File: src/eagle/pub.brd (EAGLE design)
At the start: 63.5 x 63.5 mm, 27 parts, among them IC1 PIC18F25K50, SW1 EC12E_SW

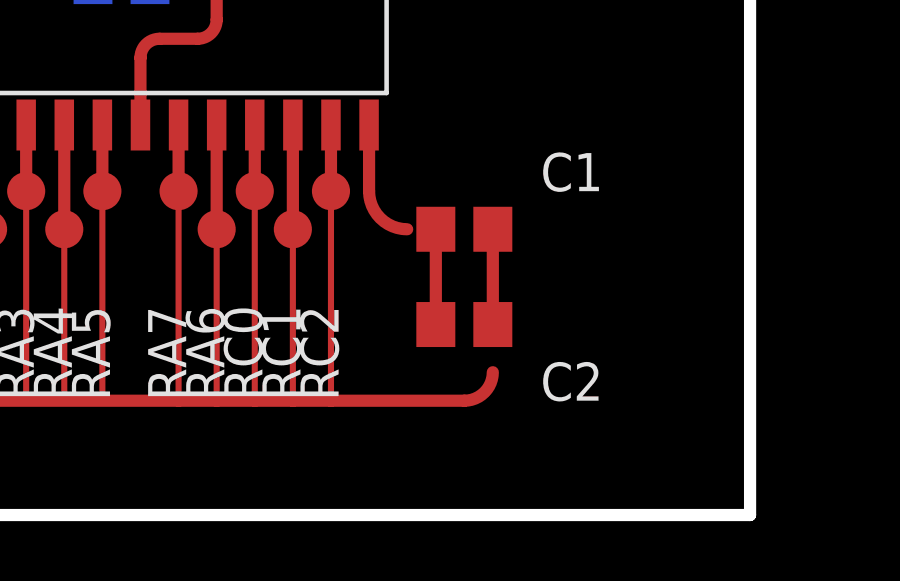
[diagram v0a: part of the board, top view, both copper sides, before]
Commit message: Fixed unconnected trace on PCB. The ITEAD guys found it. I don't know how it missed that.
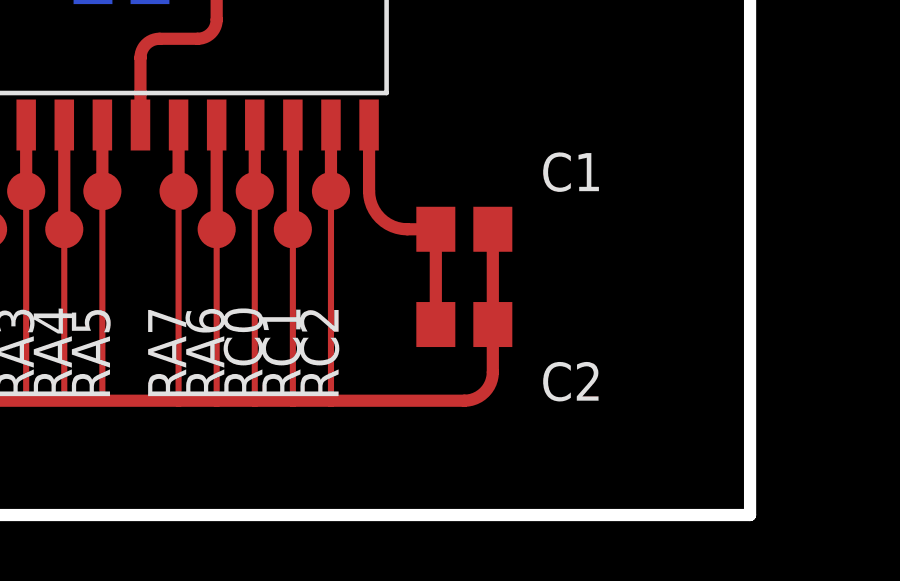
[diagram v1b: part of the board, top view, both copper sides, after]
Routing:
- net GND: track 252.9 -> 254.5 mm
- net N$3: track 7.18 -> 8.13 mm
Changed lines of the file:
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@@
 <layer number="17" name="Pads" color="2" fill="1" visible="yes" active="yes"/>
 <layer number="18" name="Vias" color="12" fill="1" visible="yes" active="yes"/>
-<layer number="19" name="Unrouted" color="6" fill="1" visible="no" active="yes"/>
+<layer number="19" name="Unrouted" color="6" fill="1" visible="yes" active="yes"/>
 <layer number="20" name="Dimension" color="15" fill="1" visible="yes" active="yes"/>
 <layer number="21" name="tPlace" color="15" fill="1" visible="no" active="yes"/>
@@
 <via x="38.1" y="31.75" extent="1-16" drill="0.4064"/>
 <wire x1="38.1" y1="31.75" x2="32.9" y2="31.75" width="0.4064" layer="16"/>
-<wire x1="54.925" y1="4.76" x2="53.975" y2="3.81" width="0.4064" layer="1" curve="-90"/>
 <wire x1="45.72" y1="16.51" x2="45.72" y2="17.78" width="0.4064" layer="1"/>
 <contactref element="JP1" pad="5"/>
@@
 <contactref element="IC1" pad="8"/>
 <wire x1="43.18" y1="13" x2="43.18" y2="15.24" width="0.4064" layer="1"/>
-<wire x1="43.18" y1="13" x2="44.45" y2="13" width="0" layer="19" extent="1-1"/>
+<wire x1="53.975" y1="3.81" x2="54.925" y2="4.76" width="0.4064" layer="1" curve="90"/>
+<wire x1="54.925" y1="4.76" x2="54.925" y2="6.35" width="0.4064" layer="1"/>
+<wire x1="44.45" y1="13" x2="43.18" y2="13" width="0" layer="19" extent="1-1"/>
 </signal>
 <signal name="N$1">
@@
 <wire x1="50.8" y1="10.795" x2="52.07" y2="9.525" width="0.4064" layer="1" curve="90"/>
 <wire x1="53.025" y1="9.525" x2="53.025" y2="6.35" width="0.4064" layer="1"/>
-<wire x1="53.025" y1="9.525" x2="52.07" y2="9.525" width="0" layer="19" extent="1-1"/>
+<wire x1="52.07" y1="9.525" x2="53.025" y2="9.525" width="0.4064" layer="1"/>
 </signal>
 </signals>

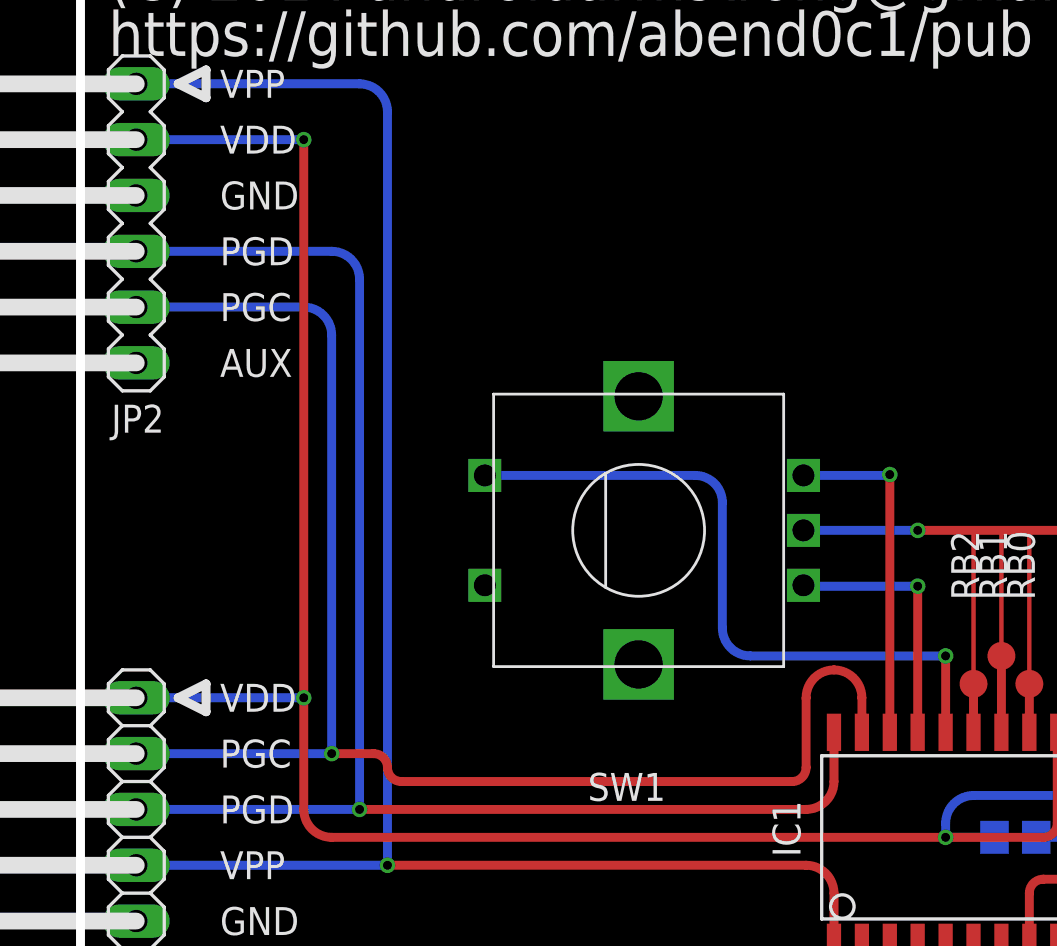
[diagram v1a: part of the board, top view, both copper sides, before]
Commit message: Reworked PCB layout and changed to vector fonts
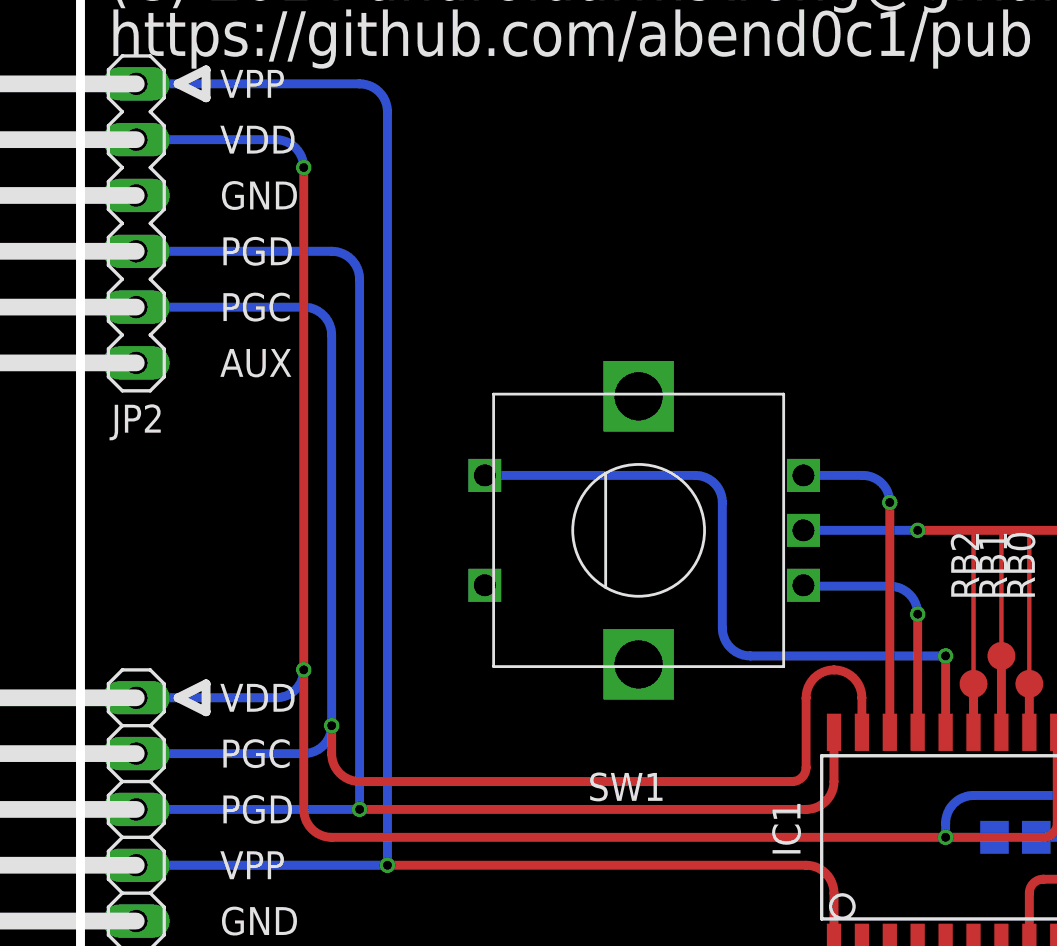
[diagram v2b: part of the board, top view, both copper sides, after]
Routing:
- net N$2: track 11.9 -> 11.1 mm
- net N$1: track 15.7 -> 14.9 mm
- net N$8: track 68.1 -> 68.6 mm

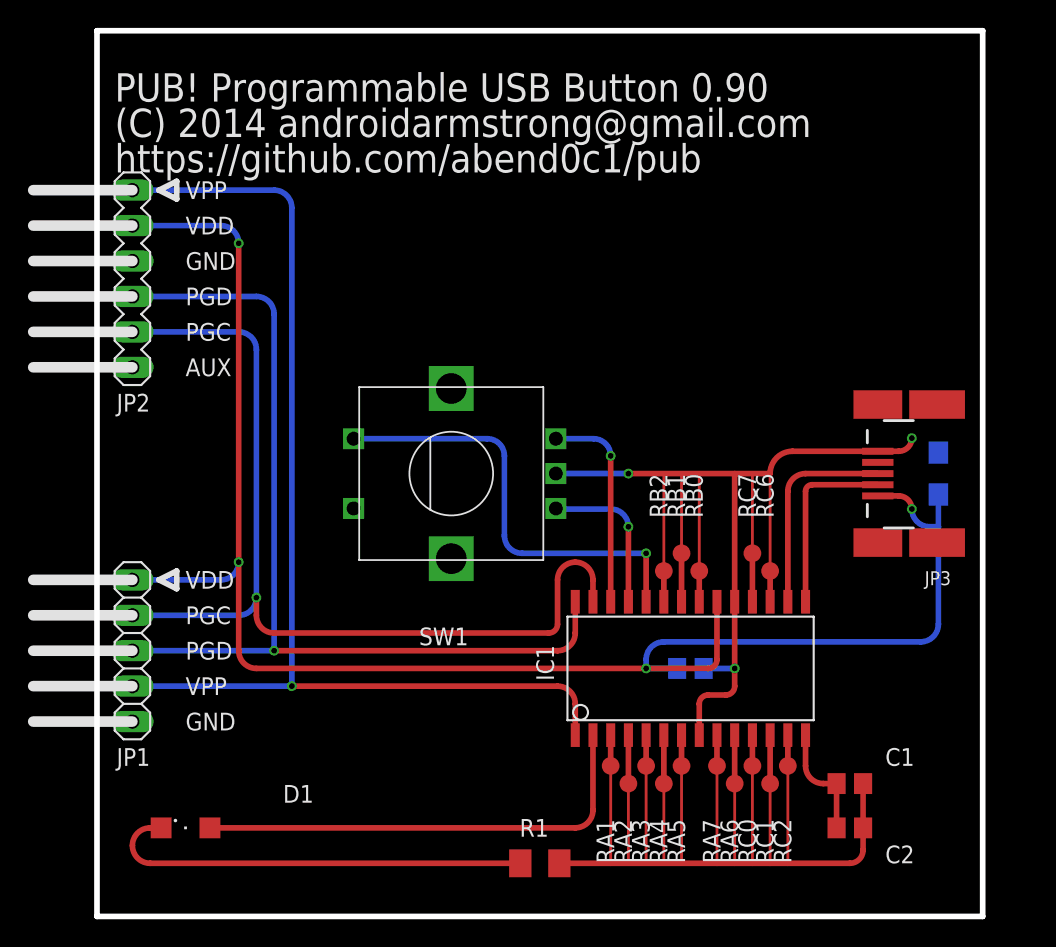
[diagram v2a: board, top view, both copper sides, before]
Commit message: Fixed PCB to match code. Rotary button on RB6
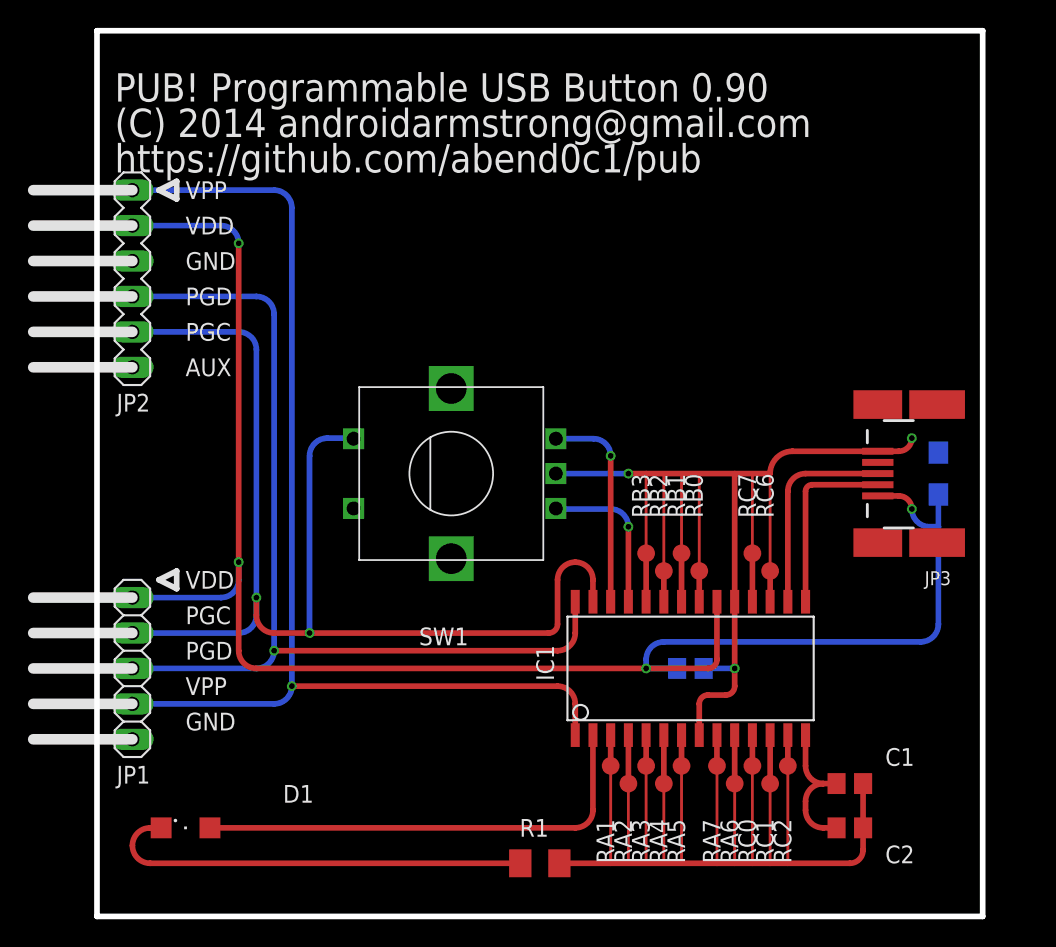
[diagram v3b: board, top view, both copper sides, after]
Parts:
- added RB3: TPB1,27, testpad:B1,27
- moved JP1 1.27 mm to (2.54, 17.8)
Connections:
- removed net RA1: IC1.24, SW1.E
- net GND: now also IC1.24, RB3.TP
- net N$8: now also SW1.E
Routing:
- net RA1: track 31.2 -> 0.00 mm, vias 1 -> 0
- net N$8: track 68.6 -> 86.3 mm, vias 1 -> 2
- net GND: track 254.5 -> 267.2 mm
- net N$3: track 8.13 -> 10.1 mm
- net N$7: track 124.1 -> 125.4 mm
- net N$9: track 69.3 -> 69.9 mm
- net N$10: track 80.8 -> 81.3 mm
